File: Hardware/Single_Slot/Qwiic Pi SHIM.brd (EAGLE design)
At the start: 10.2 x 14 mm, 14 parts, among them J1 Qwiic Right Angle, U2 3.3V/600mA

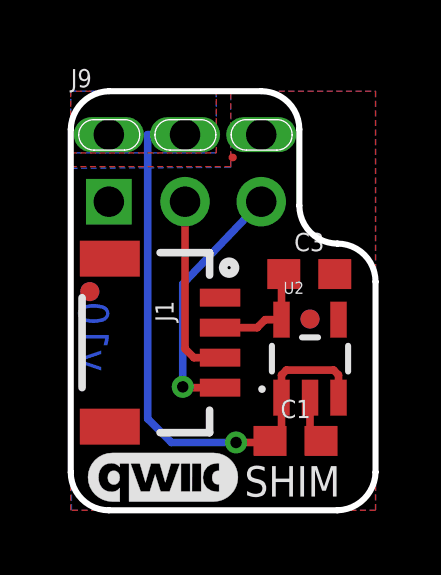
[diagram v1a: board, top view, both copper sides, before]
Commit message: adjusted dimensions to match single to double
-this lets a small amount of gnd pour around the corner.
-moved fiductials
-added gnd vias
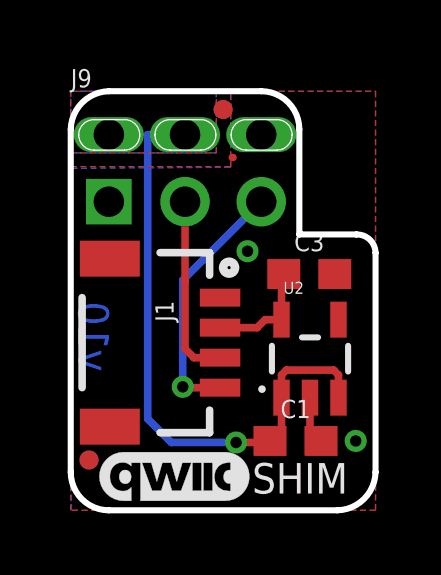
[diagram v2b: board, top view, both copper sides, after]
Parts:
- moved FD2 8.74 mm to (0.61, 1.68)
- moved FD3 8.74 mm to (0.61, 1.68)
- moved FD1 7.52 mm to (5.08, 13.4)
- moved FD4 7.52 mm to (5.08, 13.4)
- moved LOGO1 0.76 mm to (2.59, 1.63)
- moved U$3 0.38 mm to (3.43, 1.14)
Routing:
- net GND: vias 0 -> 2
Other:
- outline, holes or cut-outs redrawn
